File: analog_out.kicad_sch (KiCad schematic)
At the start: 12 parts, among them U3 TSB582

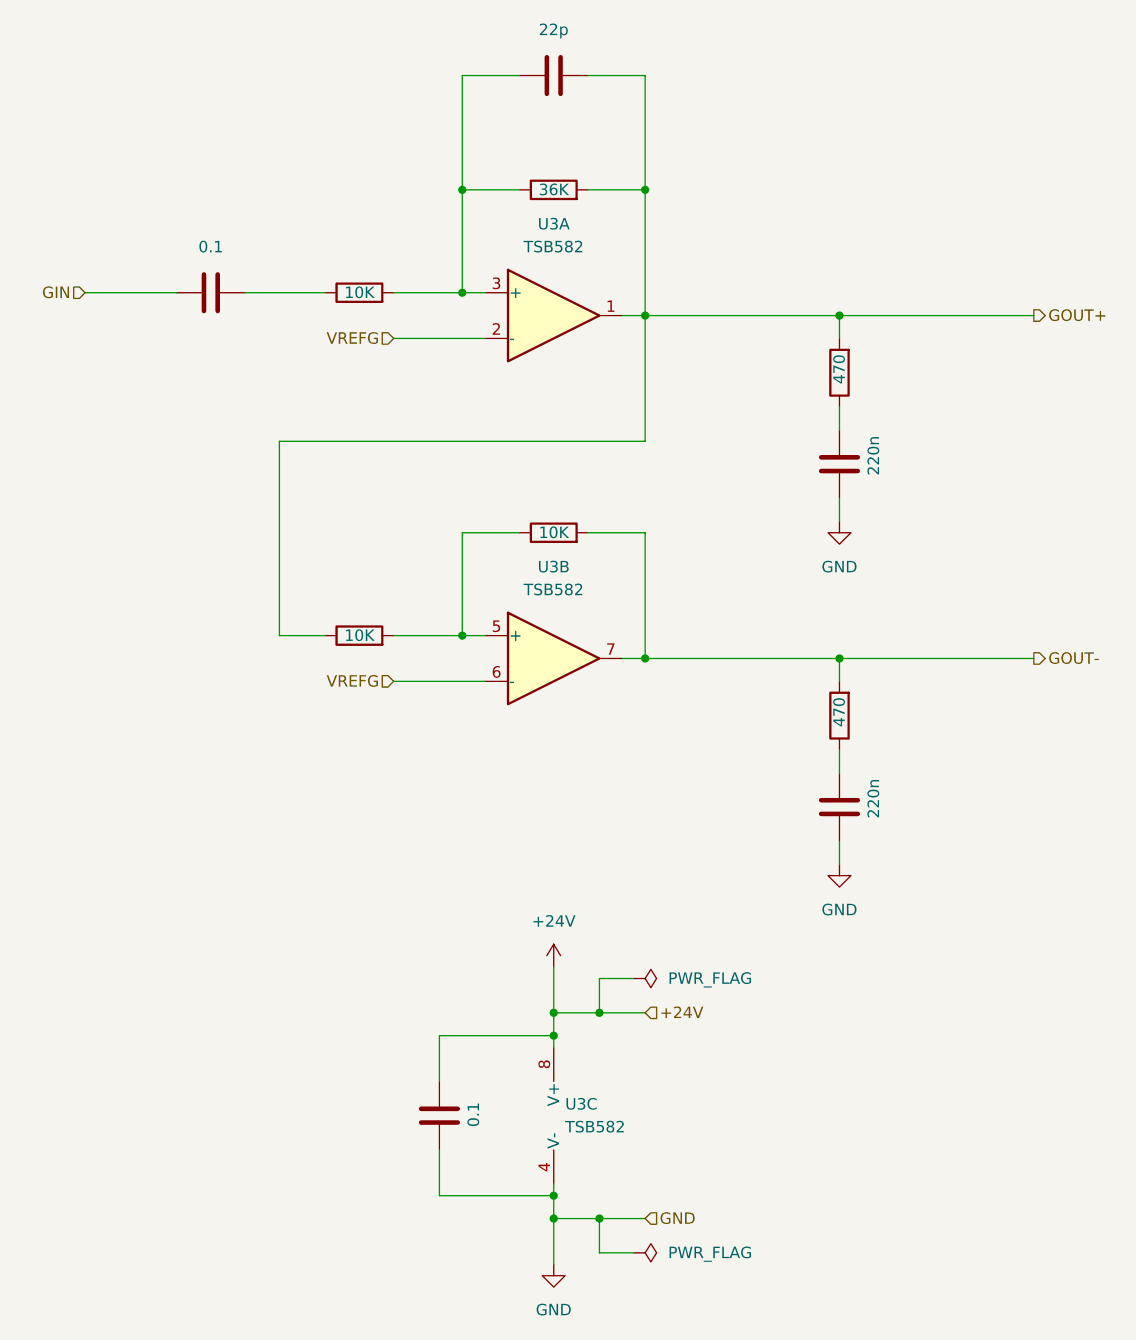
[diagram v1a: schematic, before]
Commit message: Finished power setup and cleared some mistakes
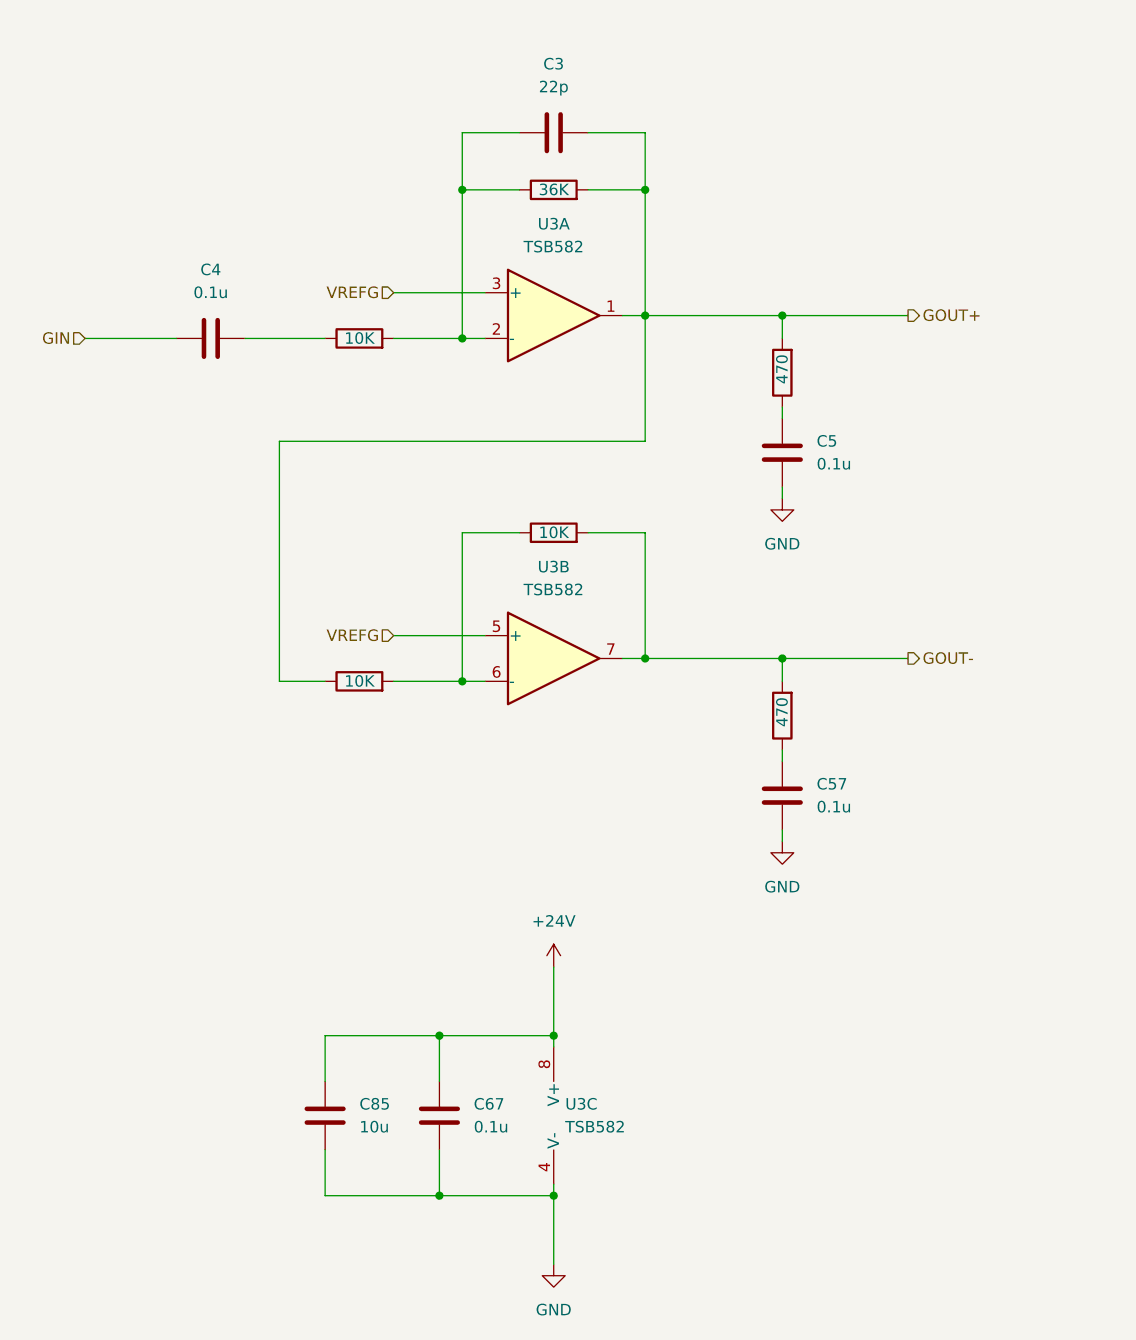
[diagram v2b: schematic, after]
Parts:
- removed C6: 220n, symbol Device:C
- removed C7: 0.1, symbol Device:C
- added C57, C67: 0.1u, symbol Device:C
- added C85: 10u, symbol Device:C
- C4: value 0.1 -> 0.1u
- C5: value 220n -> 0.1u
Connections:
- net +24V: now also C67.2, C85.2
- net GND: now also C57.1, C67.1, C85.1
- net VREFG: now also U3.3 (+), U3.5 (+); no longer U3.2 (-), U3.6 (-)
- net at R20.1: now also C57.2
- net at C3.1, R15.1, R16.2: now also U3.2 (-); no longer U3.3 (+)
- net at R18.1, R19.2: now also U3.6 (-); no longer U3.5 (+)

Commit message: Polished IO schematics
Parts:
- removed C85: 10u, symbol Device:C
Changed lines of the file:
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@@
   (junction (at 135.89 59.69) (diameter 0) (color 0 0 0 0)
   )
-  (junction (at 133.35 154.94) (diameter 0) (color 0 0 0 0)
-  )
   (junction (at 171.45 57.15) (diameter 0) (color 0 0 0 0)
   )
   (junction (at 135.89 97.79) (diameter 0) (color 0 0 0 0)
   )
-  (junction (at 133.35 137.16) (diameter 0) (color 0 0 0 0)
-  )
   (junction (at 156.21 57.15) (diameter 0) (color 0 0 0 0)
   )
   (junction (at 156.21 95.25) (diameter 0) (color 0 0 0 0)
   )
-  (wire (pts (xy 120.65 149.86) (xy 120.65 154.94))
-    (stroke (width 0) (type default))
-  )
   (wire (pts (xy 171.45 105.41) (xy 171.45 106.68))
     (stroke (width 0) (type default))
@@
     (stroke (width 0) (type default))
   )
-  (wire (pts (xy 120.65 137.16) (xy 120.65 142.24))
-    (stroke (width 0) (type default))
-  )
   (wire (pts (xy 93.98 59.69) (xy 104.14 59.69))
     (stroke (width 0) (type default))
@@
     (stroke (width 0) (type default))
   )
-  (wire (pts (xy 133.35 137.16) (xy 120.65 137.16))
-    (stroke (width 0) (type default))
-  )
   (wire (pts (xy 153.67 57.15) (xy 156.21 57.15))
     (stroke (width 0) (type default))
   )
   (wire (pts (xy 156.21 71.12) (xy 115.57 71.12))
-    (stroke (width 0) (type default))
-  )
-  (wire (pts (xy 120.65 154.94) (xy 133.35 154.94))
     (stroke (width 0) (type default))
   )
@@
         )
       )
-    )
-  )
-  (symbol (lib_id "Device:C") (at 120.65 146.05 180) (unit 1)
-    (in_bom yes) (on_board yes) (dnp no) (fields_autoplaced)
-    (property "Reference" "C85" (at 124.46 144.78 0)
-      (effects (font (size 1.27 1.27)) (justify right))
-    )
-    (property "Value" "10u" (at 124.46 147.32 0)
-      (effects (font (size 1.27 1.27)) (justify right))
-    )
-    (property "Footprint" "" (at 119.6848 142.24 0)
-      (effects (font (size 1.27 1.27)) hide)
-    )
-    (property "Datasheet" "~" (at 120.65 146.05 0)
-      (effects (font (size 1.27 1.27)) hide)
-    )
-    (pin "2")
-    (pin "1")
-    (instances
-      (project "cad-enc-dec"
-        (path "/894df1c3-1a5d-48b0-9966-84d5c2c2c705/93e1db63-c38b-43d2-ba3c-0dfe20099ed9"
-          (reference "C85") (unit 1)
-        )
-        (path "/894df1c3-1a5d-48b0-9966-84d5c2c2c705/c4705af4-6f61-4247-98e1-c8f7bbff342e"
-          (reference "C86") (unit 1)
-        )
-        (path "/894df1c3-1a5d-48b0-9966-84d5c2c2c705/4f4fa3ca-d26c-469a-8efe-defd05d53334"
-          (reference "C95") (unit 1)
-        )
-        (path "/894df1c3-1a5d-48b0-9966-84d5c2c2c705/f4af41cf-cb77-423b-ae97-ab85a1a314a5"
-          (reference "C96") (unit 1)
-        )
-        (path "/894df1c3-1a5d-48b0-9966-84d5c2c2c705/b521e4c8-6928-4f6f-bb2d-871435ac90d6"
-          (reference "C97") (unit 1)
-        )
-        (path "/894df1c3-1a5d-48b0-9966-84d5c2c2c705/bb4b6c41-e151-4e21-8b6f-2af0baac31fd"
-          (reference "C98") (unit 1)
-        )
-      )

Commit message: Assigned proper footprints for all components
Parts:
- added C137: 10u, Capacitor_SMD:C_1206_3216Metric_Pad1.33x1.80mm_HandSolder, symbol Device:C
- C3: value 22p -> 30p; footprint (none) -> Capacitor_SMD:C_0603_1608Metric_Pad1.08x0.95mm_HandSolder
- C4, C5, C57, C67: value 0.1u -> 100n; footprint (none) -> Capacitor_SMD:C_0603_1608Metric_Pad1.08x0.95mm_HandSolder
- R15, R16, R17, R18, R19, R20: footprint (none) -> Resistor_SMD:R_0603_1608Metric_Pad0.98x0.95mm_HandSolder
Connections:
- net +24V: now also C137.2
- net GND: now also C137.1
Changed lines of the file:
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@@
   (junction (at 146.05 154.94) (diameter 0) (color 0 0 0 0)
   )
+  (junction (at 133.35 137.16) (diameter 0) (color 0 0 0 0)
+  )
   (junction (at 135.89 59.69) (diameter 0) (color 0 0 0 0)
   )
   (junction (at 171.45 57.15) (diameter 0) (color 0 0 0 0)
   )
+  (junction (at 133.35 154.94) (diameter 0) (color 0 0 0 0)
+  )
   (junction (at 135.89 97.79) (diameter 0) (color 0 0 0 0)
   )
@@
     (stroke (width 0) (type default))
   )
+  (wire (pts (xy 120.65 149.86) (xy 120.65 154.94))
+    (stroke (width 0) (type default))
+  )
   (wire (pts (xy 156.21 57.15) (xy 171.45 57.15))
     (stroke (width 0) (type default))
@@
     (stroke (width 0) (type default))
   )
+  (wire (pts (xy 133.35 137.16) (xy 120.65 137.16))
+    (stroke (width 0) (type default))
+  )
   (wire (pts (xy 128.27 59.69) (xy 135.89 59.69))
     (stroke (width 0) (type default))
@@
     (stroke (width 0) (type default))
   )
+  (wire (pts (xy 120.65 137.16) (xy 120.65 142.24))
+    (stroke (width 0) (type default))
+  )
   (wire (pts (xy 135.89 59.69) (xy 138.43 59.69))
     (stroke (width 0) (type default))
@@
   )
   (wire (pts (xy 171.45 76.2) (xy 171.45 77.47))
+    (stroke (width 0) (type default))
+  )
+  (wire (pts (xy 120.65 154.94) (xy 133.35 154.94))
     (stroke (width 0) (type default))
   )
@@
       (effects (font (size 1.27 1.27)) (justify right) hide)
     )
-    (property "Value" "470" (at 171.45 102.87 90)
+    (property "Value" "470" (at 171.5565 103.5117 90)
       (effects (font (size 1.27 1.27)) (justify right))
     )
-    (property "Footprint" "" (at 173.228 101.6 90)
+    (property "Footprint" "Resistor_SMD:R_0603_1608Metric_Pad0.98x0.95mm_HandSolder" (at 173.228 101.6 90)
       (effects (font (size 1.27 1.27)) hide)
     )
@@
       (effects (font (size 1.27 1.27)))
     )
-    (property "Footprint" "" (at 146.05 44.958 90)
+    (property "Footprint" "Resistor_SMD:R_0603_1608Metric_Pad0.98x0.95mm_HandSolder" (at 146.05 44.958 90)
       (effects (font (size 1.27 1.27)) hide)
     )
@@
       (effects (font (size 1.27 1.27)) (justify right))
     )
-    (property "Value" "0.1u" (at 175.26 73.66 0)
+    (property "Value" "100n" (at 175.26 73.66 0)
       (effects (font (size 1.27 1.27)) (justify right))
     )
-    (property "Footprint" "" (at 170.4848 68.58 0)
+    (property "Footprint" "Capacitor_SMD:C_0603_1608Metric_Pad1.08x0.95mm_HandSolder" (at 170.4848 68.58 0)
       (effects (font (size 1.27 1.27)) hide)
     )
@@
       (effects (font (size 1.27 1.27)) (justify right) hide)
     )
-    (property "Value" "470" (at 171.45 64.77 90)
+    (property "Value" "470" (at 171.5036 65.4357 90)
       (effects (font (size 1.27 1.27)) (justify right))
     )
-    (property "Footprint" "" (at 173.228 63.5 90)
+    (property "Footprint" "Resistor_SMD:R_0603_1608Metric_Pad0.98x0.95mm_HandSolder" (at 173.228 63.5 90)
       (effects (font (size 1.27 1.27)) hide)
     )
@@
       (effects (font (size 1.27 1.27)))
     )
-    (property "Value" "22p" (at 146.05 31.75 90)
-      (effects (font (size 1.27 1.27)))
-    )
-    (property "Footprint" "" (at 149.86 35.8648 0)
+    (property "Value" "30p" (at 146.05 31.75 90)
+      (effects (font (size 1.27 1.27)))
+    )
+    (property "Footprint" "Capacitor_SMD:C_0603_1608Metric_Pad1.08x0.95mm_HandSolder" (at 149.86 35.8648 0)
       (effects (font (size 1.27 1.27)) hide)
     )
@@
       (effects (font (size 1.27 1.27)))
     )
-    (property "Footprint" "" (at 124.46 61.468 90)
+    (property "Footprint" "Resistor_SMD:R_0603_1608Metric_Pad0.98x0.95mm_HandSolder" (at 124.46 61.468 90)
       (effects (font (size 1.27 1.27)) hide)
     )
@@
       (effects (font (size 1.27 1.27)))
     )
-    (property "Value" "0.1u" (at 107.95 54.61 90)
-      (effects (font (size 1.27 1.27)))
-    )
-    (property "Footprint" "" (at 111.76 58.7248 0)
+    (property "Value" "100n" (at 107.95 54.61 90)
+      (effects (font (size 1.27 1.27)))
+    )
+    (property "Footprint" "Capacitor_SMD:C_0603_1608Metric_Pad1.08x0.95mm_HandSolder" (at 111.76 58.7248 0)
       (effects (font (size 1.27 1.27)) hide)
     )
@@
       (effects (font (size 1.27 1.27)) (justify right))
     )
-    (property "Value" "0.1u" (at 175.26 111.76 0)
+    (property "Value" "100n" (at 175.26 111.76 0)
       (effects (font (size 1.27 1.27)) (justify right))
     )
-    (property "Footprint" "" (at 170.4848 106.68 0)
+    (property "Footprint" "Capacitor_SMD:C_0603_1608Metric_Pad1.08x0.95mm_HandSolder" (at 170.4848 106.68 0)
       (effects (font (size 1.27 1.27)) hide)
     )
@@
       (effects (font (size 1.27 1.27)))
     )
-    (property "Footprint" "" (at 146.05 83.058 90)
+    (property "Footprint" "Resistor_SMD:R_0603_1608Metric_Pad0.98x0.95mm_HandSolder" (at 146.05 83.058 90)
       (effects (font (size 1.27 1.27)) hide)
     )
@@
     )
   )
+  (symbol (lib_id "Device:C") (at 120.65 146.05 180) (unit 1)
+    (in_bom yes) (on_board yes) (dnp no) (fields_autoplaced)
+    (property "Reference" "C137" (at 124.46 144.78 0)
+      (effects (font (size 1.27 1.27)) (justify right))
+    )
+    (property "Value" "10u" (at 124.46 147.32 0)
+      (effects (font (size 1.27 1.27)) (justify right))
+    )
+    (property "Footprint" "Capacitor_SMD:C_1206_3216Metric_Pad1.33x1.80mm_HandSolder" (at 119.6848 142.24 0)
+      (effects (font (size 1.27 1.27)) hide)
+    )
+    (property "Datasheet" "~" (at 120.65 146.05 0)
+      (effects (font (size 1.27 1.27)) hide)
+    )
+    (pin "2")
+    (pin "1")
+    (instances
+      (project "cad-enc-dec"
+        (path "/894df1c3-1a5d-48b0-9966-84d5c2c2c705/93e1db63-c38b-43d2-ba3c-0dfe20099ed9"
+          (reference "C137") (unit 1)
+        )
+        (path "/894df1c3-1a5d-48b0-9966-84d5c2c2c705/c4705af4-6f61-4247-98e1-c8f7bbff342e"
+          (reference "C138") (unit 1)
+        )
+        (path "/894df1c3-1a5d-48b0-9966-84d5c2c2c705/4f4fa3ca-d26c-469a-8efe-defd05d53334"
+          (reference "C139") (unit 1)
+        )
+        (path "/894df1c3-1a5d-48b0-9966-84d5c2c2c705/f4af41cf-cb77-423b-ae97-ab85a1a314a5"
+          (reference "C140") (unit 1)
+        )
+        (path "/894df1c3-1a5d-48b0-9966-84d5c2c2c705/b521e4c8-6928-4f6f-bb2d-871435ac90d6"
+          (reference "C141") (unit 1)
+        )
+        (path "/894df1c3-1a5d-48b0-9966-84d5c2c2c705/bb4b6c41-e151-4e21-8b6f-2af0baac31fd"
+          (reference "C142") (unit 1)
+        )
+      )
+    )
+  )
   (symbol (lib_id "Device:C") (at 133.35 146.05 180) (unit 1)
     (in_bom yes) (on_board yes) (dnp no) (fields_autoplaced)
@@
       (effects (font (size 1.27 1.27)) (justify right))
     )
-    (property "Value" "0.1u" (at 137.16 147.32 0)
+    (property "Value" "100n" (at 137.16 147.32 0)
       (effects (font (size 1.27 1.27)) (justify right))
     )
-    (property "Footprint" "" (at 132.3848 142.24 0)
+    (property "Footprint" "Capacitor_SMD:C_0603_1608Metric_Pad1.08x0.95mm_HandSolder" (at 132.3848 142.24 0)
       (effects (font (size 1.27 1.27)) hide)
     )
@@
       (effects (font (size 1.27 1.27)))
     )
-    (property "Footprint" "" (at 124.46 99.568 90)
-      (effects (font (size 1.27 1.27)) hide)
-    )
+    (property "Footprint" "Resistor_SMD:R_0603_1608Metric_Pad0.98x0.95mm_HandSolder" (at 124.46 99.568 90)
+      (effects (font (size 1.27 1.27)) hide)
+    )

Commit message: Updated boards hierarchy
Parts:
- renumbered C3 to C51, C4 to C52, C5 to C53, C57 to C54, C137 to C55, C67 to C56, R15 to R161, R16 to R162, R17 to R163, R18 to R164, R19 to R165, R20 to R166, U3 to U63

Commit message: Finished annotation
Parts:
- renumbered C51 to C3701, C52 to C3702, C53 to C3703, C54 to C3704, C55 to C3705, C56 to C3706, R161 to R3701, R162 to R3702, R163 to R3703, R164 to R3704, R165 to R3705, R166 to R3706, U63 to U3701

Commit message: Merged receiver and transmitter
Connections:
- net GIN renamed AOUT
- net GOUT+ renamed AOUT+
- net GOUT- renamed AOUT-
- net VREFG renamed VREFA
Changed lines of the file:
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@@
     (stroke (width 0) (type default))
   )
-  (hierarchical_label "GOUT-" (shape output) (at 185.42 95.25 0) (fields_autoplaced)
+  (hierarchical_label "AOUT-" (shape output) (at 185.42 95.25 0) (fields_autoplaced)
     (effects (font (size 1.27 1.27)) (justify left))
   )
-  (hierarchical_label "VREFG" (shape input) (at 128.27 92.71 180) (fields_autoplaced)
+  (hierarchical_label "VREFA" (shape input) (at 128.27 92.71 180) (fields_autoplaced)
     (effects (font (size 1.27 1.27)) (justify right))
   )
-  (hierarchical_label "GOUT+" (shape output) (at 185.42 57.15 0) (fields_autoplaced)
+  (hierarchical_label "AOUT+" (shape output) (at 185.42 57.15 0) (fields_autoplaced)
     (effects (font (size 1.27 1.27)) (justify left))
   )
-  (hierarchical_label "VREFG" (shape input) (at 128.27 54.61 180) (fields_autoplaced)
+  (hierarchical_label "VREFA" (shape input) (at 128.27 54.61 180) (fields_autoplaced)
     (effects (font (size 1.27 1.27)) (justify right))
   )
-  (hierarchical_label "GIN" (shape input) (at 93.98 59.69 180) (fields_autoplaced)
+  (hierarchical_label "AOUT" (shape input) (at 93.98 59.69 180) (fields_autoplaced)
     (effects (font (size 1.27 1.27)) (justify right))
   )

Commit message: Split schematic into three subprojects
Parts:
- renumbered C3701 to C43, C3702 to C44, C3703 to C45, C3704 to C46, C3705 to C47, C3706 to C48, R3701 to R55, R3702 to R56, R3703 to R57, R3704 to R58, R3705 to R59, R3706 to R60, U3701 to U24
